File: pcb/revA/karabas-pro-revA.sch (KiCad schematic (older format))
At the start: 127 parts, among them CON1 CF-CARD, CON2 SD, CON3 VGA, CON4 Joystick, CON5 Keyboard, CON6 Mouse, CON7 Audio, CON8 5V DC, J1 Floppy, J2 FPGA JTAG, J3 Floppy 5V, J4 uBus, J5 AVR JTAG, J6 AVR UART, SW1 SW_Push, SW2 SW_Push, U1 EP4CE6E22C8N, U10 ESP-12E, U11 TDA1543, U12 AMS1117-3.3, U13 AMS1117-2.5, U14 AMS1117-1.2, U17 74LS06, U18 74LS38, U2 CY62167EV30, U3 W25Q32JVSS, U4 EPM3128ATC100-5, U5 ATMEGA328-AU, U6 MB8877A, U7 TXB0104PW, U8 TXB0104PW, U9 DS1307Z+, X1 SG-7050CAN, Y1 32768Hz, Y2 16MHz

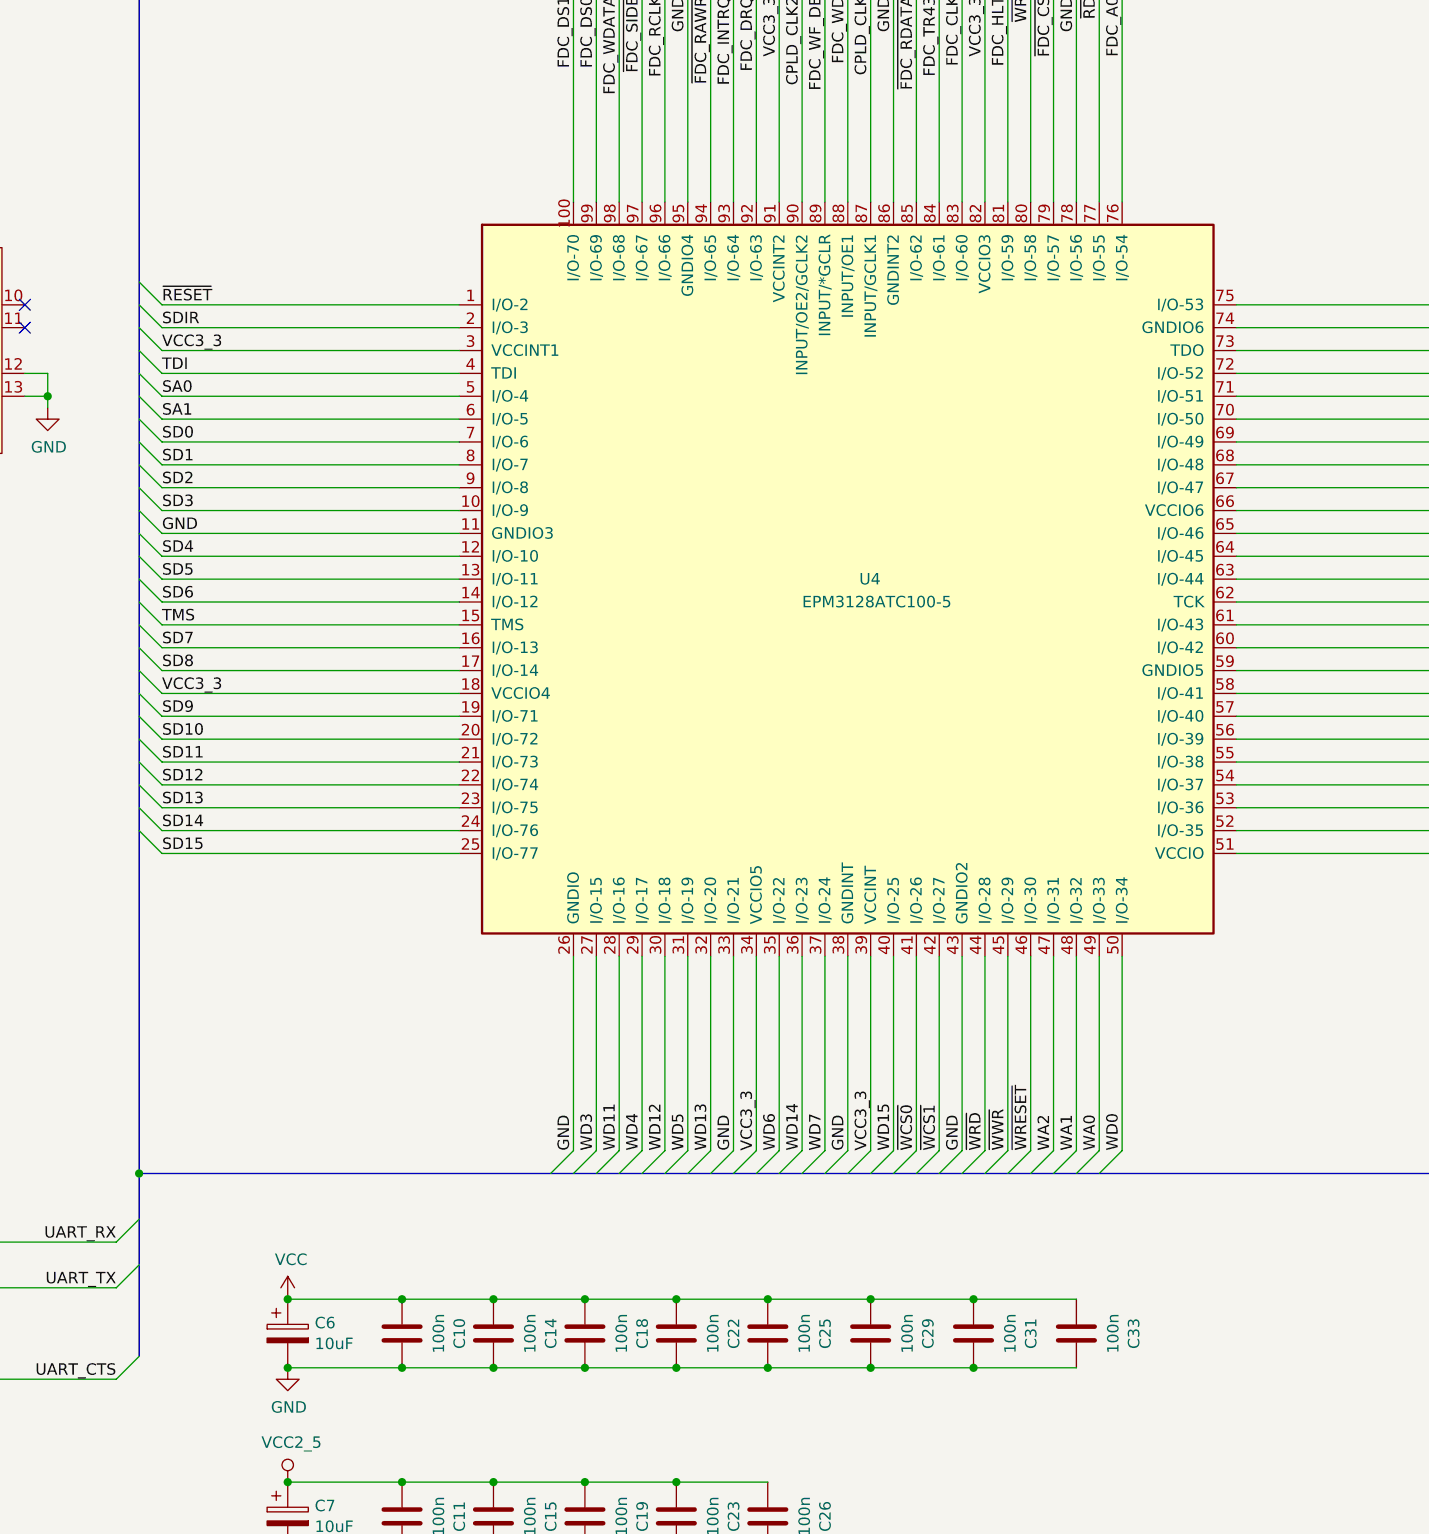
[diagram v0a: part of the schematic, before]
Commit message: Added pullups
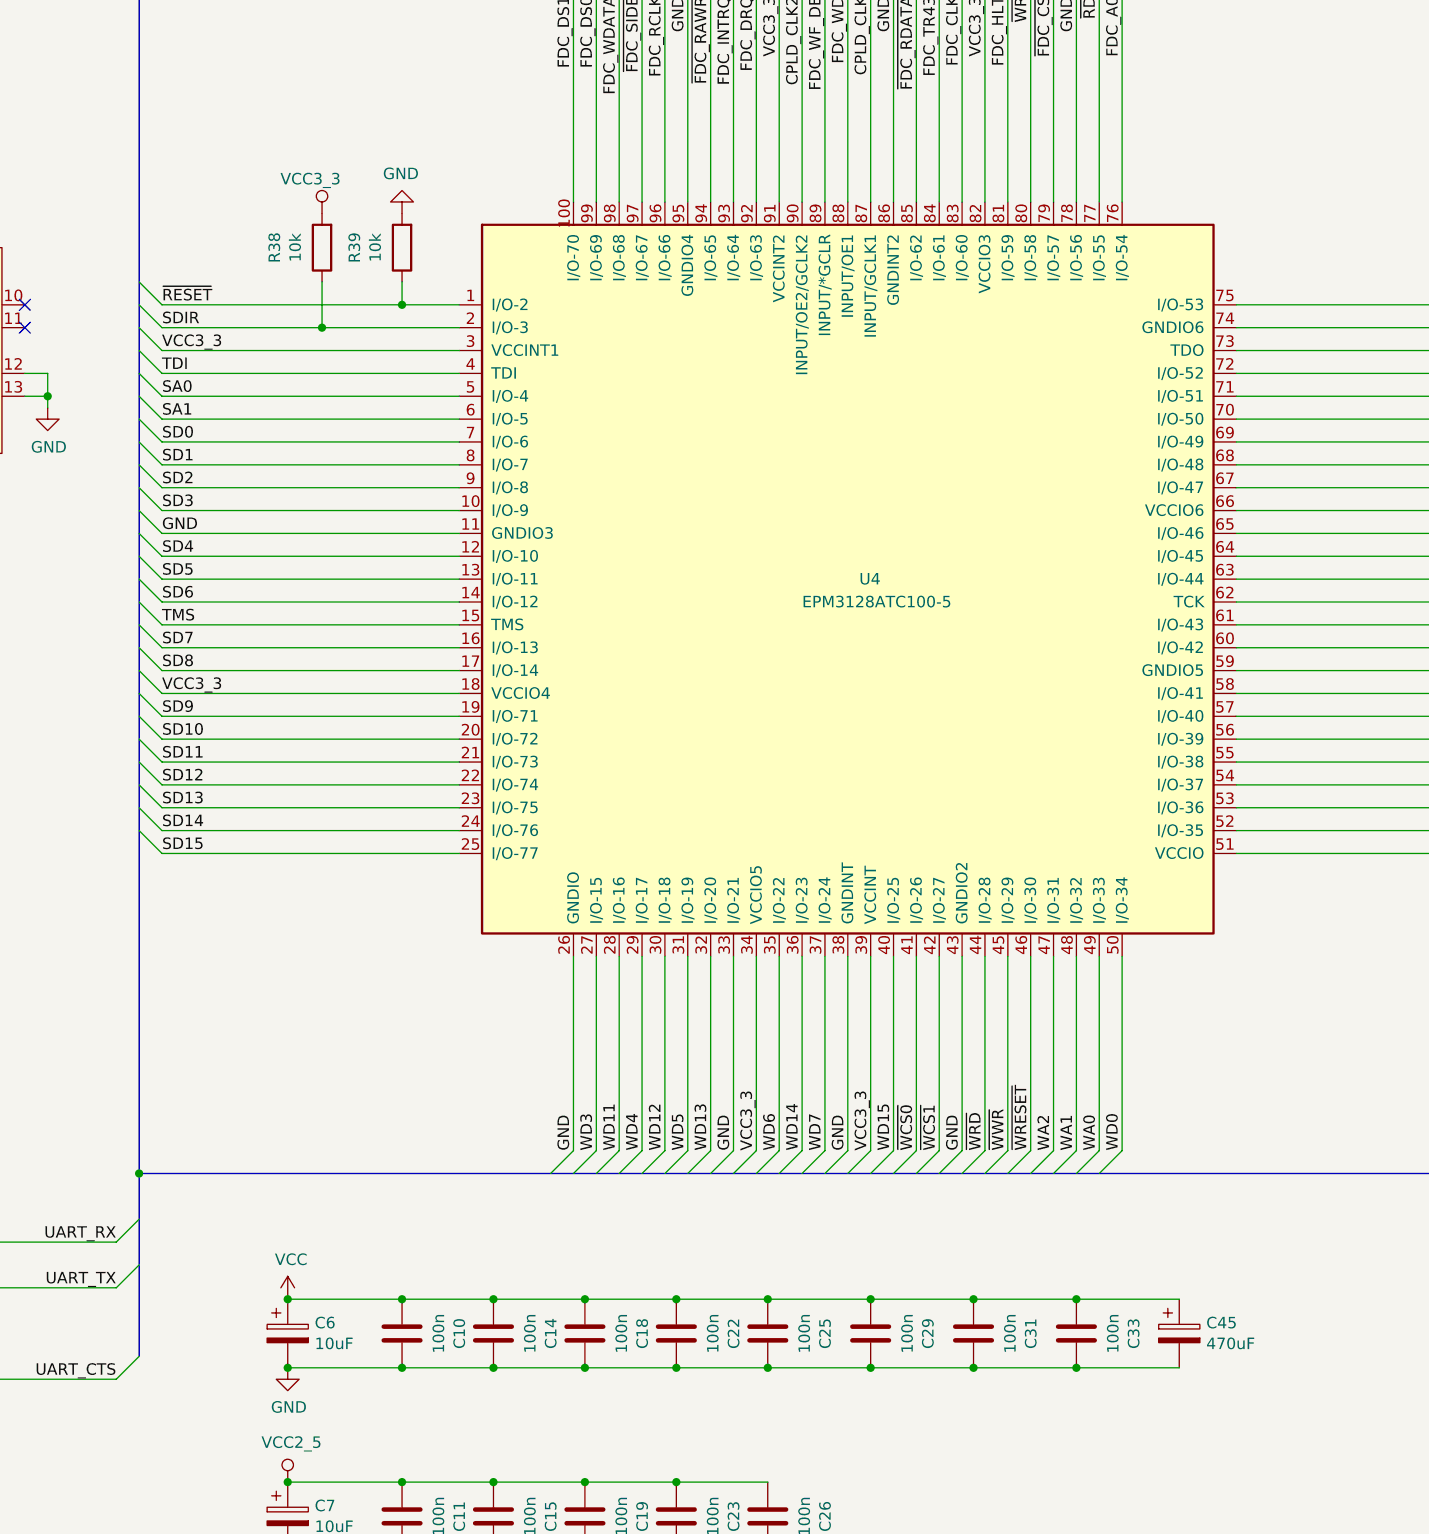
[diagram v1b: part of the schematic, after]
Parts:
- added C45: 470uF, Capacitor_THT:CP_Radial_D12.5mm_P7.50mm, symbol Device:CP
- added R38, R39: 10k, Resistor_SMD:R_0805_2012Metric_Pad1.15x1.40mm_HandSolder, symbol Device:R
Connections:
- net GND: now also C45.2, R39.2
- net SDIR: now also R38.1
- net VCC: now also C45.1
- net VCC3_3: now also R38.2
- net ~RESET: now also R39.1
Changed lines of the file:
@@
 	14300 6600 15600 6600
 Wire Wire Line
-	15600 6500 14300 6500
-Wire Wire Line
-	14300 6400 15600 6400
+	15600 6500 15000 6500
+Wire Wire Line
+	14300 6400 15350 6400
 Text Label 14300 8800 0    50   ~ 0
 SD15
@@
 Text Label 11150 3700 0    50   ~ 0
 AVR_TX
+$Comp
+L Device:R R39
+U 1 1 5EFD4192
+P 15350 6150
+F 0 "R39" V 15557 6150 50  0000 C CNN
+F 1 "10k" V 15466 6150 50  0000 C CNN
+F 2 "Resistor_SMD:R_0805_2012Metric_Pad1.15x1.40mm_HandSolder" V 15280 6150 50  0001 C CNN
+F 3 "~" H 15350 6150 50  0001 C CNN
+	1    15350 6150
+	-1   0    0    1
+$EndComp
+$Comp
+L power:GND #PWR0175
+U 1 1 5EFD6432
+P 15350 6000
+F 0 "#PWR0175" H 15350 5750 50  0001 C CNN
+F 1 "GND" H 15355 5827 50  0000 C CNN
+F 2 "" H 15350 6000 50  0001 C CNN
+F 3 "" H 15350 6000 50  0001 C CNN
+	1    15350 6000
+	-1   0    0    1
+$EndComp
+Wire Wire Line
+	15350 6300 15350 6400
+Connection ~ 15350 6400
+Wire Wire Line
+	15350 6400 15600 6400
+$Comp
+L Device:R R38
+U 1 1 5F203B49
+P 15000 6150
+F 0 "R38" V 15207 6150 50  0000 C CNN
+F 1 "10k" V 15116 6150 50  0000 C CNN
+F 2 "Resistor_SMD:R_0805_2012Metric_Pad1.15x1.40mm_HandSolder" V 14930 6150 50  0001 C CNN
+F 3 "~" H 15000 6150 50  0001 C CNN
+	1    15000 6150
+	-1   0    0    1
+$EndComp
+$Comp
+L vcc33:VCC3_3 #PWR0176
+U 1 1 5F204E83
+P 15000 6000
+F 0 "#PWR0176" H 15000 5850 50  0001 C CNN
+F 1 "VCC3_3" H 14950 6150 50  0000 C CNN
+F 2 "" H 15000 6000 50  0001 C CNN
+F 3 "" H 15000 6000 50  0001 C CNN
+	1    15000 6000
+	1    0    0    -1
+$EndComp
+Wire Wire Line
+	15000 6300 15000 6500
+Connection ~ 15000 6500
+Wire Wire Line
+	15000 6500 14300 6500
+$Comp
+L Device:CP C45
+U 1 1 5F3013A0
+P 18750 10900
+F 0 "C45" H 18868 10946 50  0000 L CNN
+F 1 "470uF" H 18868 10855 50  0000 L CNN
+F 2 "Capacitor_THT:CP_Radial_D12.5mm_P7.50mm" H 18788 10750 50  0001 C CNN
+F 3 "~" H 18750 10900 50  0001 C CNN
+	1    18750 10900
+	1    0    0    -1
+$EndComp
+Wire Wire Line
+	18750 10750 18300 10750
+Connection ~ 18300 10750
+Wire Wire Line
+	18750 11050 18300 11050
 Wire Bus Line
 	14200 10200 14200 11000
@@
 Wire Bus Line
 	8750 700  8750 11450
+Connection ~ 18300 11050
 $EndSCHEMATC
